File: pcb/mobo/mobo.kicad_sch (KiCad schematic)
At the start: 73 parts, among them J1 ISP, J2 PEEL_MOTOR, J3 DRIVE_MOTOR, J5 SPRING_FINGERS, J8 USART1, U1 ATmega328PB-A, U2 ATmega328PB-M, U3 LED_RGB, U4 AP1117-50, U5 MC34063AD, U6 SP308xE, U7 DRV8837, U8 DRV8837, Y1 16MHz

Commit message: Rearrange schematic and add annotations
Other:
- note added: ""Backwards" button"
- note added: ""Forwards" button"
- note added: "120 Ohm termination resistor needed at the end of the bus. This should be present on the motherboard, and on the 50th slot PCB."
- note added: "Alternate footprint for the MCU to help alleviate stockout issues with the main QFP package"
- note added: "DRIVE MOTOR CONTROL"
- note added: "Keeps motor drivers disabled when the MCU is in bootloader mode. Peel motor spins might spin in bootloader mode without this pulldown."
- note added: "PEEL MOTOR CONTROL"
- note added: "Status LED Alternate footprint marked as DNP in case of main LED stockout."
- note added: "UART port for programming"
- note removed: "120 Ohm termination resistor needed at the end of the bus"
- note removed: "MOTOR CONTROL"
- moved on the sheet: C1, C10, C12, C13, C14, C16, C17, C18, C19, C2, C20, C22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

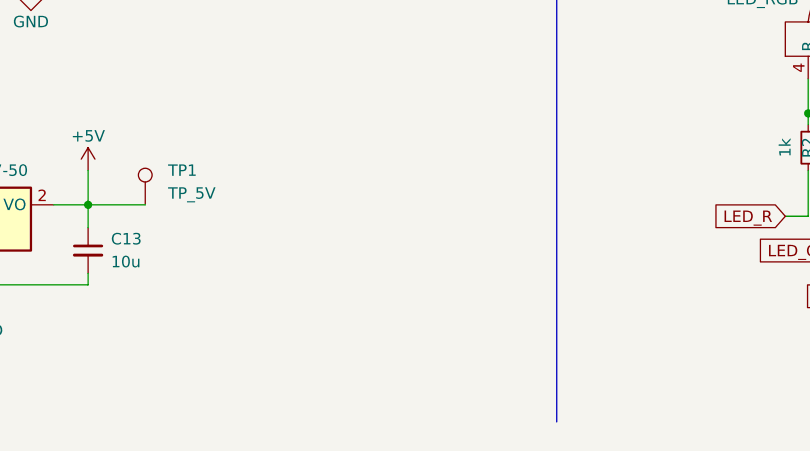
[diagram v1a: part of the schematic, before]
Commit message: Add power flags to mobo to fix ERC errors
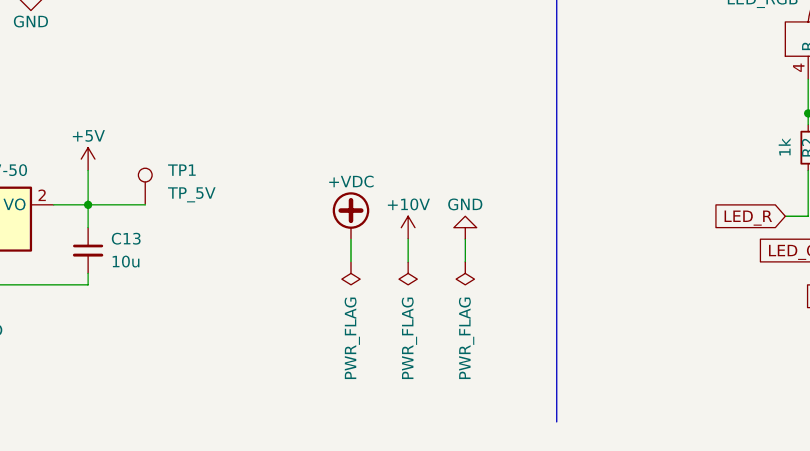
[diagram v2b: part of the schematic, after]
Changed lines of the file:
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@@
     (stroke (width 0) (type default))
   )
+  (wire (pts (xy 121.92 262.89) (xy 121.92 265.43))
+    (stroke (width 0) (type default))
+  )
   (polyline (pts (xy 12.7 180.34) (xy 252.73 180.34))
     (stroke (width 0) (type default))
@@
     (stroke (width 0) (type default))
   )
+  (wire (pts (xy 115.57 262.89) (xy 115.57 265.43))
+    (stroke (width 0) (type default))
+  )
   (wire (pts (xy 342.9 163.83) (xy 351.79 163.83))
     (stroke (width 0) (type default))
@@
     (stroke (width 0) (type default))
   )
+  (wire (pts (xy 109.22 262.89) (xy 109.22 265.43))
+    (stroke (width 0) (type default))
+  )
   (wire (pts (xy 170.18 257.81) (xy 172.72 257.81))
     (stroke (width 0) (type default))
@@
     )
   )
+  (symbol (lib_id "power:PWR_FLAG") (at 109.22 265.43 180) (unit 1)
+    (in_bom yes) (on_board yes) (dnp no)
+    (property "Reference" "#FLG01" (at 109.22 267.335 0)
+      (effects (font (size 1.27 1.27)) hide)
+    )
+    (property "Value" "PWR_FLAG" (at 109.22 269.24 90)
+      (effects (font (size 1.27 1.27)) (justify left))
+    )
+    (property "Footprint" "" (at 109.22 265.43 0)
+      (effects (font (size 1.27 1.27)) hide)
+    )
+    (property "Datasheet" "~" (at 109.22 265.43 0)
+      (effects (font (size 1.27 1.27)) hide)
+    )
+    (pin "1")
+    (instances
+      (project "mobo"
+        (path "/e502d1d5-04b0-4d4b-b5c3-8c52d09668e7"
+          (reference "#FLG01") (unit 1)
+        )
+      )
+    )
+  )
   (symbol (lib_id "power:GND") (at 73.66 234.95 0) (unit 1)
     (in_bom yes) (on_board yes) (dnp no)
@@
     )
   )
+  (symbol (lib_id "power:+10V") (at 115.57 262.89 0) (unit 1)
+    (in_bom yes) (on_board yes) (dnp no)
+    (property "Reference" "#PWR04" (at 115.57 266.7 0)
+      (effects (font (size 1.27 1.27)) hide)
+    )
+    (property "Value" "+10V" (at 115.57 259.08 0)
+      (effects (font (size 1.27 1.27)))
+    )
+    (property "Footprint" "" (at 115.57 262.89 0)
+      (effects (font (size 1.27 1.27)) hide)
+    )
+    (property "Datasheet" "" (at 115.57 262.89 0)
+      (effects (font (size 1.27 1.27)) hide)
+    )
+    (pin "1")
+    (instances
+      (project "mobo"
+        (path "/e502d1d5-04b0-4d4b-b5c3-8c52d09668e7"
+          (reference "#PWR04") (unit 1)
+        )
+      )
+    )
+  )
+  (symbol (lib_id "power:GND") (at 121.92 262.89 180) (unit 1)
+    (in_bom yes) (on_board yes) (dnp no)
+    (property "Reference" "#PWR05" (at 121.92 256.54 0)
+      (effects (font (size 1.27 1.27)) hide)
+    )
+    (property "Value" "GND" (at 121.92 259.08 0)
+      (effects (font (size 1.27 1.27)))
+    )
+    (property "Footprint" "" (at 121.92 262.89 0)
+      (effects (font (size 1.27 1.27)) hide)
+    )
+    (property "Datasheet" "" (at 121.92 262.89 0)
+      (effects (font (size 1.27 1.27)) hide)
+    )
+    (pin "1")
+    (instances
+      (project "mobo"
+        (path "/e502d1d5-04b0-4d4b-b5c3-8c52d09668e7"
+          (reference "#PWR05") (unit 1)
+        )
+      )
+    )
+  )
   (symbol (lib_id "power:+VDC") (at 43.18 209.55 0) (unit 1)
     (in_bom yes) (on_board yes) (dnp no)
@@
     )
   )
+  (symbol (lib_id "power:PWR_FLAG") (at 121.92 265.43 180) (unit 1)
+    (in_bom yes) (on_board yes) (dnp no)
+    (property "Reference" "#FLG03" (at 121.92 267.335 0)
+      (effects (font (size 1.27 1.27)) hide)
+    )
+    (property "Value" "PWR_FLAG" (at 121.92 269.24 90)
+      (effects (font (size 1.27 1.27)) (justify left))
+    )
+    (property "Footprint" "" (at 121.92 265.43 0)
+      (effects (font (size 1.27 1.27)) hide)
+    )
+    (property "Datasheet" "~" (at 121.92 265.43 0)
+      (effects (font (size 1.27 1.27)) hide)
+    )
+    (pin "1")
+    (instances
+      (project "mobo"
+        (path "/e502d1d5-04b0-4d4b-b5c3-8c52d09668e7"
+          (reference "#FLG03") (unit 1)
+        )
+      )
+    )
+  )
   (symbol (lib_id "power:GND") (at 339.09 118.11 0) (unit 1)
     (in_bom yes) (on_board yes) (dnp no)
@@
     )
   )
+  (symbol (lib_id "power:+VDC") (at 109.22 262.89 0) (unit 1)
+    (in_bom yes) (on_board yes) (dnp no)
+    (property "Reference" "#PWR03" (at 109.22 265.43 0)
+      (effects (font (size 1.27 1.27)) hide)
+    )
+    (property "Value" "+VDC" (at 109.22 256.54 0)
+      (effects (font (size 1.27 1.27)))
+    )
+    (property "Footprint" "" (at 109.22 262.89 0)
+      (effects (font (size 1.27 1.27)) hide)
+    )
+    (property "Datasheet" "" (at 109.22 262.89 0)
+      (effects (font (size 1.27 1.27)) hide)
+    )
+    (pin "1")
+    (instances
+      (project "mobo"
+        (path "/e502d1d5-04b0-4d4b-b5c3-8c52d09668e7"
+          (reference "#PWR03") (unit 1)
+        )
+      )
+    )
+  )
   (symbol (lib_id "Connector:TestPoint") (at 49.53 259.08 0) (unit 1)
     (in_bom yes) (on_board yes) (dnp no)
@@
         )
       )
+    )
+  )
+  (symbol (lib_id "power:PWR_FLAG") (at 115.57 265.43 180) (unit 1)
+    (in_bom yes) (on_board yes) (dnp no)
+    (property "Reference" "#FLG02" (at 115.57 267.335 0)
+      (effects (font (size 1.27 1.27)) hide)
+    )
+    (property "Value" "PWR_FLAG" (at 115.57 269.24 90)
+      (effects (font (size 1.27 1.27)) (justify left))
+    )
+    (property "Footprint" "" (at 115.57 265.43 0)
+      (effects (font (size 1.27 1.27)) hide)
+    )
+    (property "Datasheet" "~" (at 115.57 265.43 0)
+      (effects (font (size 1.27 1.27)) hide)
+    )
+    (pin "1")
+    (instances
+      (project "mobo"
+        (path "/e502d1d5-04b0-4d4b-b5c3-8c52d09668e7"
+          (reference "#FLG02") (unit 1)
+        )
+      )
